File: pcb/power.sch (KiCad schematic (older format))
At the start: 15 parts, among them U6 USBMICROCONN

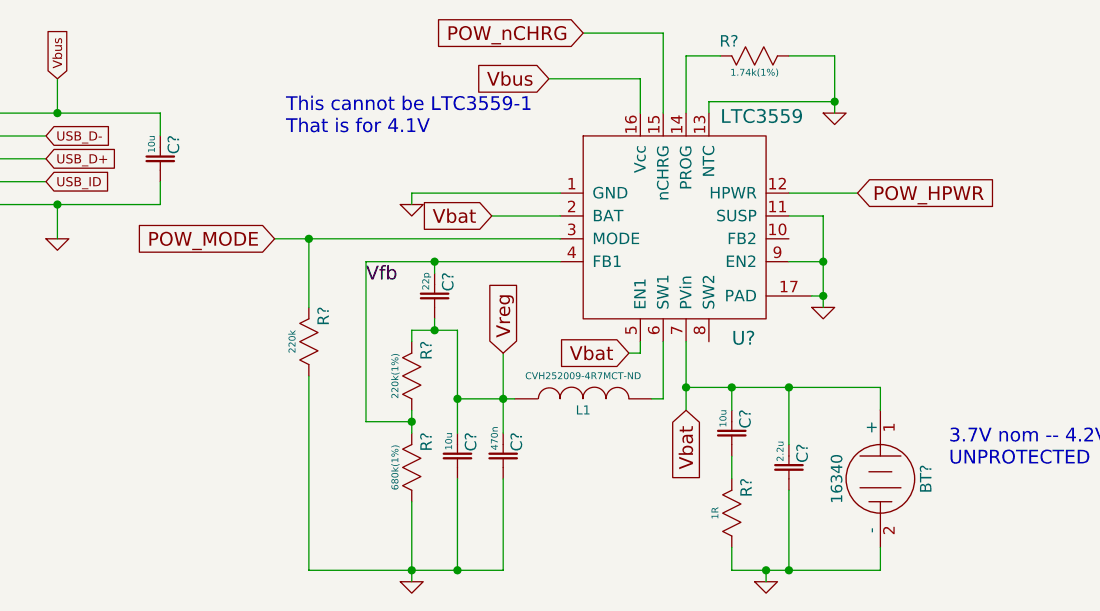
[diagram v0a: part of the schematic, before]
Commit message: Added LCD and started wiring busses
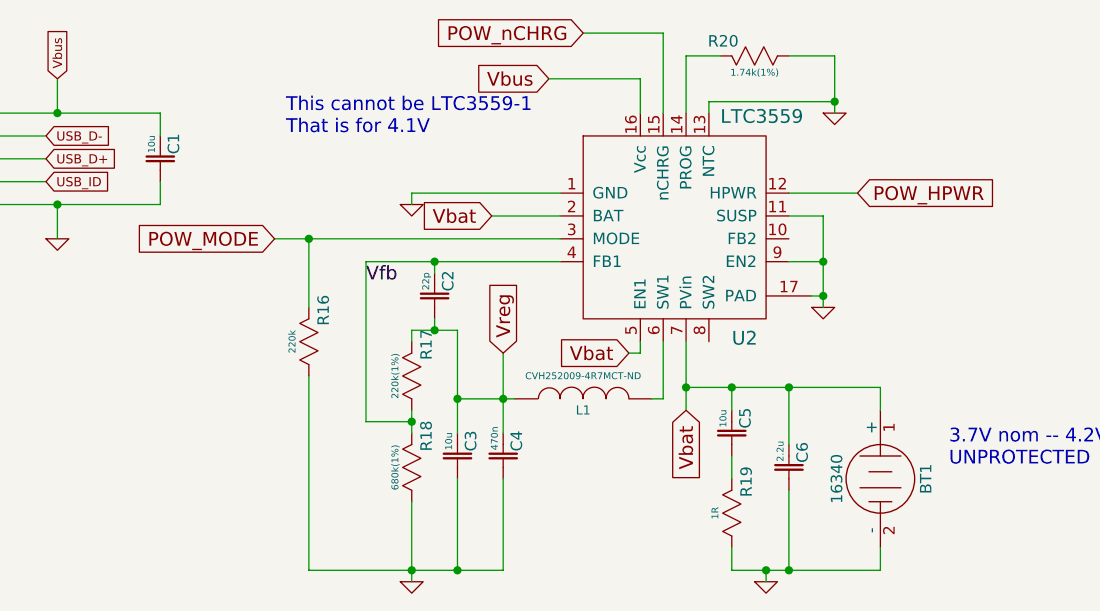
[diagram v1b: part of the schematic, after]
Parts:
- gave numbers to parts that had none: 13
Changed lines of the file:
@@
-EESchema Schematic File Version 2  date Thu 26 Jul 2012 02:08:52 PM EDT
+EESchema Schematic File Version 2  date Thu 26 Jul 2012 11:54:13 PM EDT
 LIBS:power
 LIBS:device
@@
 EELAYER 25  0
 EELAYER END
-$Descr A4 11700 8267
+$Descr A4 11693 8268
 encoding utf-8
 Sheet 4 5
 Title ""
-Date "26 jul 2012"
+Date "27 jul 2012"
 Rev ""
 Comp ""
@@
 Connection ~ 5900 3300
 $Comp
-L BATTERY BT?
+L BATTERY BT1
 U 1 1 501184C6
 P 6300 3700
-F 0 "BT?" H 6300 3900 50  0000 C CNN
+F 0 "BT1" H 6300 3900 50  0000 C CNN
 F 1 "16340" H 6300 3510 50  0000 C CNN
 	1    6300 3700
@@
 $EndComp
 $Comp
-L GND #PWR?
+L GND #PWR21
 U 1 1 50117654
 P 5800 4150
-F 0 "#PWR?" H 5800 4150 30  0001 C CNN
+F 0 "#PWR21" H 5800 4150 30  0001 C CNN
 F 1 "GND" H 5800 4080 30  0001 C CNN
 	1    5800 4150
@@
 $EndComp
 $Comp
-L CAP C?
+L CAP C3
 U 1 1 5011763D
 P 4450 3600
-F 0 "C?" H 4470 3570 50  0000 L TNN
+F 0 "C3" H 4470 3570 50  0000 L TNN
 F 1 "10u" H 4475 3620 30  0000 L BNN
 	1    4450 3600
@@
 $EndComp
 $Comp
-L CAP C?
+L CAP C6
 U 1 1 5011763B
 P 5900 3650
-F 0 "C?" H 5920 3620 50  0000 L TNN
+F 0 "C6" H 5920 3620 50  0000 L TNN
 F 1 "2.2u" H 5925 3670 30  0000 L BNN
 	1    5900 3650
@@
 POW_MODE
 $Comp
-L RES R?
+L RES R16
 U 1 1 501174F2
 P 3800 3100
-F 0 "R?" H 3870 3065 50  0000 L TNN
+F 0 "R16" H 3870 3065 50  0000 L TNN
 F 1 "220k" H 3800 3155 30  0000 C BNN
 	1    3800 3100
@@
 $EndComp
 $Comp
-L RES R?
+L RES R19
 U 1 1 5011722B
 P 5650 3850
-F 0 "R?" H 5720 3815 50  0000 L TNN
+F 0 "R19" H 5720 3815 50  0000 L TNN
 F 1 "1R" H 5650 3905 30  0000 C BNN
 	1    5650 3850
@@
 $EndComp
 $Comp
-L CAP C?
+L CAP C1
 U 1 1 50116F2D
 P 3150 2300
-F 0 "C?" H 3170 2270 50  0000 L TNN
+F 0 "C1" H 3170 2270 50  0000 L TNN
 F 1 "10u" H 3175 2320 30  0000 L BNN
 	1    3150 2300
@@
 Vbat
 $Comp
-L CAP C?
+L CAP C4
 U 1 1 50116EB4
 P 4650 3600
-F 0 "C?" H 4670 3570 50  0000 L TNN
+F 0 "C4" H 4670 3570 50  0000 L TNN
 F 1 "470n" H 4675 3620 30  0000 L BNN
 	1    4650 3600
@@
 $EndComp
 $Comp
-L CAP C?
+L CAP C2
 U 1 1 50116E87
 P 4350 2900
-F 0 "C?" H 4370 2870 50  0000 L TNN
+F 0 "C2" H 4370 2870 50  0000 L TNN
 F 1 "22p" H 4375 2920 30  0000 L BNN
 	1    4350 2900
@@
 Vreg
 $Comp
-L CAP C?
+L CAP C5
 U 1 1 50116E51
 P 5650 3500
-F 0 "C?" H 5670 3470 50  0000 L TNN
+F 0 "C5" H 5670 3470 50  0000 L TNN
 F 1 "10u" H 5675 3520 30  0000 L BNN
 	1    5650 3500
@@
 Vbus
 $Comp
-L GND #PWR?
+L GND #PWR23
 U 1 1 50116DE1
 P 6100 2100
-F 0 "#PWR?" H 6100 2100 30  0001 C CNN
+F 0 "#PWR23" H 6100 2100 30  0001 C CNN
 F 1 "GND" H 6100 2030 30  0001 C CNN
 	1    6100 2100
@@
 $EndComp
 $Comp
-L RES R?
+L RES R20
 U 1 1 50116DC3
 P 5750 1850
-F 0 "R?" H 5820 1815 50  0000 L TNN
+F 0 "R20" H 5820 1815 50  0000 L TNN
 F 1 "1.74k(1%)" H 5750 1905 30  0000 C BNN
 	1    5750 1850
@@
 Vfb
 $Comp
-L GND #PWR?
+L GND #PWR20
 U 1 1 50116D88
 P 4250 4150
-F 0 "#PWR?" H 4250 4150 30  0001 C CNN
+F 0 "#PWR20" H 4250 4150 30  0001 C CNN
 F 1 "GND" H 4250 4080 30  0001 C CNN
 	1    4250 4150
@@
 $EndComp
 $Comp
-L RES R?
+L RES R18
 U 1 1 50116D7E
 P 4250 3650
-F 0 "R?" H 4320 3615 50  0000 L TNN
+F 0 "R18" H 4320 3615 50  0000 L TNN
 F 1 "680k(1%)" H 4250 3705 30  0000 C BNN
 	1    4250 3650
@@
 $EndComp
 $Comp
-L RES R?
+L RES R17
 U 1 1 50116D75
 P 4250 3250
-F 0 "R?" H 4320 3215 50  0000 L TNN
+F 0 "R17" H 4320 3215 50  0000 L TNN
 F 1 "220k(1%)" H 4250 3305 30  0000 C BNN
 	1    4250 3250
@@
 Vbat
 $Comp
-L GND #PWR?
+L GND #PWR22
 U 1 1 50116D38
 P 6050 2950
-F 0 "#PWR?" H 6050 2950 30  0001 C CNN
+F 0 "#PWR22" H 6050 2950 30  0001 C CNN
 F 1 "GND" H 6050 2880 30  0001 C CNN
 	1    6050 2950
@@
 $EndComp
 $Comp
-L GND #PWR?
+L GND #PWR19
 U 1 1 50116D32
 P 4250 2500
-F 0 "#PWR?" H 4250 2500 30  0001 C CNN
+F 0 "#PWR19" H 4250 2500 30  0001 C CNN
 F 1 "GND" H 4250 2430 30  0001 C CNN
 	1    4250 2500
@@
 Vbat
 $Comp
-L LTC3559 U?
+L LTC3559 U2
 U 1 1 50116CFF
 P 5400 2600
-F 0 "U?" H 5650 2150 60  0000 L TNN
+F 0 "U2" H 5650 2150 60  0000 L TNN
 F 1 "LTC3559" H 5600 3050 60  0000 L BNN
 	1    5400 2600

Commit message: Broke up schematic in a more modular fashion -- Added LCD footprint
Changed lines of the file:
@@
-EESchema Schematic File Version 2  date Thu 26 Jul 2012 11:54:13 PM EDT
+EESchema Schematic File Version 2  date Tue 31 Jul 2012 10:29:35 PM EDT
 LIBS:power
 LIBS:device
@@
 EELAYER 25  0
 EELAYER END
-$Descr A4 11693 8268
+$Descr A4 11700 8267
 encoding utf-8
-Sheet 4 5
+Sheet 5 6
 Title ""
-Date "27 jul 2012"
+Date "1 aug 2012"
 Rev ""
 Comp ""
@@
 Comment4 ""
 $EndDescr
+Text HLabel 2650 2400 2    40   Output ~ 0
+USB_ID
+Text HLabel 2650 2300 2    40   Output ~ 0
+USB_D+
+Text HLabel 2650 2200 2    40   Output ~ 0
+USB_D-
+Text HLabel 3650 2650 0    60   Input ~ 0
+POW_MODE
+Text HLabel 5000 1750 0    60   Output ~ 0
+POW_nCHRG
+Text HLabel 6200 2450 2    60   Input ~ 0
+POW_HPWR
 Text Notes 3700 2200 0    60   ~ 0
 This cannot be LTC3559-1\nThat is for 4.1V
@@
 Connection ~ 5900 4100
 Wire Wire Line
-	6300 4100 5900 4100
-Wire Wire Line
-	5900 4100 5800 4100
-Wire Wire Line
-	5800 4100 5650 4100
+	6300 4100 5650 4100
 Wire Wire Line
 	6300 4100 6300 4000
@@
 Connection ~ 3800 2650
 Wire Wire Line
-	4900 2650 3800 2650
-Wire Wire Line
-	3800 2650 3650 2650
+	4900 2650 3650 2650
 Wire Wire Line
 	3800 2650 3800 2950
@@
 	3150 2400 3150 2500
 Wire Wire Line
-	3150 2500 2700 2500
-Wire Wire Line
-	2700 2500 2400 2500
+	3150 2500 2400 2500
 Wire Wire Line
 	3150 2200 3150 2100
@@
 	5900 1850 6100 1850
 Wire Wire Line
-	6100 1850 6100 2050
-Wire Wire Line
-	6100 2050 6100 2100
+	6100 1850 6100 2100
 Wire Wire Line
 	5600 1850 5450 1850
@@
 	5450 1850 5450 2100
 Wire Wire Line
-	4250 3800 4250 4100
-Wire Wire Line
-	4250 4100 4250 4150
+	4250 3800 4250 4150
 Wire Wire Line
 	4250 3100 4250 3050
 Wire Wire Line
-	4250 3050 4350 3050
-Wire Wire Line
-	4350 3050 4450 3050
-Wire Wire Line
-	4700 3350 4650 3350
-Wire Wire Line
-	4650 3350 4450 3350
+	4250 3050 4450 3050
+Wire Wire Line
+	4700 3350 4450 3350
 Wire Wire Line
 	5250 3100 5250 3150
@@
 	5350 3350 5350 3100
 Wire Wire Line
-	4250 3400 4250 3450
-Wire Wire Line
-	4250 3450 4250 3500
+	4250 3400 4250 3500
 Wire Wire Line
 	4250 3450 4050 3450
@@
 	4050 3450 4050 2750
 Wire Wire Line
-	4050 2750 4350 2750
-Wire Wire Line
-	4350 2750 4900 2750
+	4050 2750 4900 2750
 Wire Wire Line
 	5550 2100 5550 2050
@@
 	5250 1950 5250 2100
 Wire Wire Line
-	4450 3050 4450 3350
-Wire Wire Line
-	4450 3350 4450 3500
+	4450 3050 4450 3500
 Connection ~ 4450 3350
 Wire Wire Line
@@
 Connection ~ 4350 2750
 Wire Wire Line
-	4650 3150 4650 3350
-Wire Wire Line
-	4650 3350 4650 3500
-Wire Wire Line
-	5450 3100 5450 3300
-Wire Wire Line
-	5450 3300 5450 3400
+	4650 3150 4650 3500
+Wire Wire Line
+	5450 3100 5450 3400
 Wire Wire Line
 	2700 2650 2700 2500
 Wire Wire Line
-	3150 2100 2700 2100
-Wire Wire Line
-	2700 2100 2400 2100
+	3150 2100 2400 2100
 Wire Wire Line
 	3800 3250 3800 4100
 Wire Wire Line
-	3800 4100 4250 4100
-Wire Wire Line
-	4250 4100 4450 4100
-Wire Wire Line
-	4450 4100 4650 4100
+	3800 4100 4650 4100
 Wire Wire Line
 	5000 1750 5350 1750
@@
 	5900 2550 6050 2550
 Wire Wire Line
-	6050 2550 6050 2750
-Wire Wire Line
-	6050 2750 6050 2900
-Wire Wire Line
-	6050 2900 6050 2950
+	6050 2550 6050 2950
 Connection ~ 6050 2750
 Wire Wire Line
@@
 	6300 3400 6300 3300
 Wire Wire Line
-	6300 3300 5900 3300
-Wire Wire Line
-	5900 3300 5650 3300
-Wire Wire Line
-	5650 3300 5450 3300
+	6300 3300 5450 3300
 Connection ~ 5900 3300
 $Comp
@@
 $EndComp
 $Comp
-L GND #PWR21
+L GND #PWR020
 U 1 1 50117654
 P 5800 4150
-F 0 "#PWR21" H 5800 4150 30  0001 C CNN
+F 0 "#PWR020" H 5800 4150 30  0001 C CNN
 F 1 "GND" H 5800 4080 30  0001 C CNN
 	1    5800 4150
@@
 	0    -1   -1   0
 $EndComp
-Text GLabel 6200 2450 2    60   Input ~ 0
-POW_HPWR
-Text GLabel 5000 1750 0    60   Input ~ 0
-POW_nCHRG
-Text GLabel 3650 2650 0    60   Input ~ 0
-POW_MODE
 $Comp
 L RES R16
@@
 Vbus
 $Comp
-L GND #PWR23
+L GND #PWR021
 U 1 1 50116DE1
 P 6100 2100
-F 0 "#PWR23" H 6100 2100 30  0001 C CNN
+F 0 "#PWR021" H 6100 2100 30  0001 C CNN
 F 1 "GND" H 6100 2030 30  0001 C CNN
 	1    6100 2100
@@
 Vfb
 $Comp
-L GND #PWR20
+L GND #PWR022
 U 1 1 50116D88
 P 4250 4150
-F 0 "#PWR20" H 4250 4150 30  0001 C CNN
+F 0 "#PWR022" H 4250 4150 30  0001 C CNN
 F 1 "GND" H 4250 4080 30  0001 C CNN
 	1    4250 4150
@@
 Vbat
 $Comp
-L GND #PWR22
+L GND #PWR023
 U 1 1 50116D38
 P 6050 2950
-F 0 "#PWR22" H 6050 2950 30  0001 C CNN
+F 0 "#PWR023" H 6050 2950 30  0001 C CNN
 F 1 "GND" H 6050 2880 30  0001 C CNN
 	1    6050 2950
@@
 $EndComp
 $Comp
-L GND #PWR19
+L GND #PWR024
 U 1 1 50116D32
 P 4250 2500
-F 0 "#PWR19" H 4250 2500 30  0001 C CNN
+F 0 "#PWR024" H 4250 2500 30  0001 C CNN
 F 1 "GND" H 4250 2430 30  0001 C CNN
 	1    4250 2500
@@
 	1    0    0    -1
 $EndComp
-Text GLabel 2650 2400 2    40   Input ~ 0
-USB_ID
-Text GLabel 2650 2300 2    40   Input ~ 0
-USB_D+
-Text GLabel 2650 2200 2    40   Input ~ 0
-USB_D-
 Text GLabel 2700 1950 1    40   Input ~ 0
 Vbus
 $Comp
-L GND #PWR18
+L GND #PWR025
 U 1 1 501093EE
 P 2700 2650
-F 0 "#PWR18" H 2700 2650 30  0001 C CNN
+F 0 "#PWR025" H 2700 2650 30  0001 C CNN
 F 1 "GND" H 2700 2580 30  0001 C CNN
 	1    2700 2650

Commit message: Added step-up converter in the schematics files
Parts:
- added C? (x2): 10u, symbol CAP
- added L2: CVH252009-4R7MCT-ND, symbol INDUCTOR
- added R?: 1M, symbol RES
- added R?: 131k, symbol RES
- added U?: TLV61220, symbol TLV61220
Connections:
- net labels added: POW_NXT, Vnxt
- wire segments 60 -> 100
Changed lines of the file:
@@
-EESchema Schematic File Version 2  date Fri 07 Sep 2012 05:49:39 PM EDT
+EESchema Schematic File Version 2  date 9/9/2012 8:55:02 PM
 LIBS:power
 LIBS:device
@@
 Sheet 5 6
 Title ""
-Date "7 sep 2012"
+Date "10 sep 2012"
 Rev ""
 Comp ""
@@
 Comment4 ""
 $EndDescr
+Wire Wire Line
+	8400 2900 8700 2900
+Wire Wire Line
+	8700 2600 7700 2600
+Connection ~ 10100 2600
+Wire Wire Line
+	9900 2900 10100 2900
+Wire Wire Line
+	10000 2300 10000 2100
+Wire Wire Line
+	10000 2300 9900 2300
+Connection ~ 5900 4100
+Wire Wire Line
+	6300 4100 5900 4100
+Wire Wire Line
+	5900 4100 5800 4100
+Wire Wire Line
+	5800 4100 5650 4100
+Wire Wire Line
+	6300 4100 6300 4000
+Connection ~ 5650 3300
+Wire Wire Line
+	5900 3550 5900 3300
+Wire Wire Line
+	5650 3700 5650 3600
+Wire Wire Line
+	5900 4100 5900 3750
+Wire Wire Line
+	5800 4150 5800 4100
+Wire Wire Line
+	6200 2450 5900 2450
+Connection ~ 3800 2650
+Wire Wire Line
+	4900 2650 3800 2650
+Wire Wire Line
+	3800 2650 3650 2650
+Wire Wire Line
+	3800 2650 3800 2950
+Connection ~ 2700 2100
+Wire Wire Line
+	2700 1950 2700 2100
+Connection ~ 2700 2500
+Wire Wire Line
+	3150 2400 3150 2500
+Wire Wire Line
+	3150 2500 2700 2500
+Wire Wire Line
+	2700 2500 2400 2500
+Wire Wire Line
+	3150 2200 3150 2100
+Connection ~ 4450 4100
+Wire Wire Line
+	4650 3700 4650 4100
+Connection ~ 4350 3050
+Wire Wire Line
+	4350 3000 4350 3050
+Connection ~ 4650 3350
+Connection ~ 4250 4100
+Connection ~ 6100 2050
+Wire Wire Line
+	5900 1850 6100 1850
+Wire Wire Line
+	6100 1850 6100 2050
+Wire Wire Line
+	6100 2050 6100 2100
+Wire Wire Line
+	5600 1850 5450 1850
+Wire Wire Line
+	5450 1850 5450 2100
+Wire Wire Line
+	4250 3800 4250 4100
+Wire Wire Line
+	4250 4100 4250 4150
+Wire Wire Line
+	4250 3100 4250 3050
+Wire Wire Line
+	4250 3050 4350 3050
+Wire Wire Line
+	4350 3050 4450 3050
+Wire Wire Line
+	4700 3350 4650 3350
+Wire Wire Line
+	4650 3350 4450 3350
+Wire Wire Line
+	5250 3100 5250 3150
+Wire Wire Line
+	5250 3150 5200 3150
+Wire Wire Line
+	6050 2900 6000 2900
+Wire Wire Line
+	4900 2550 4600 2550
+Wire Wire Line
+	2650 2300 2400 2300
+Wire Wire Line
+	2650 2400 2400 2400
+Wire Wire Line
+	2400 2200 2650 2200
+Wire Wire Line
+	4250 2500 4250 2450
+Wire Wire Line
+	4250 2450 4900 2450
+Wire Wire Line
+	5900 2750 6050 2750
+Connection ~ 6050 2900
+Wire Wire Line
+	5300 3350 5350 3350
+Wire Wire Line
+	5350 3350 5350 3100
+Wire Wire Line
+	4250 3400 4250 3450
+Wire Wire Line
+	4250 3450 4250 3500
+Wire Wire Line
+	4250 3450 4050 3450
+Connection ~ 4250 3450
+Wire Wire Line
+	4050 3450 4050 2750
+Wire Wire Line
+	4050 2750 4350 2750
+Wire Wire Line
+	4350 2750 4900 2750
+Wire Wire Line
+	5550 2100 5550 2050
+Wire Wire Line
+	5550 2050 6100 2050
+Wire Wire Line
+	4850 1950 5250 1950
+Wire Wire Line
+	5250 1950 5250 2100
+Wire Wire Line
+	4450 3050 4450 3350
+Wire Wire Line
+	4450 3350 4450 3500
+Connection ~ 4450 3350
+Wire Wire Line
+	4350 2800 4350 2750
+Connection ~ 4350 2750
+Wire Wire Line
+	4650 3150 4650 3350
+Wire Wire Line
+	4650 3350 4650 3500
+Wire Wire Line
+	5450 3100 5450 3300
+Wire Wire Line
+	5450 3300 5450 3400
+Wire Wire Line
+	2700 2650 2700 2500
+Wire Wire Line
+	3150 2100 2700 2100
+Wire Wire Line
+	2700 2100 2400 2100
+Wire Wire Line
+	3800 3250 3800 4100
+Wire Wire Line
+	3800 4100 4250 4100
+Wire Wire Line
+	4250 4100 4450 4100
+Wire Wire Line
+	4450 4100 4650 4100
+Wire Wire Line
+	5000 1750 5350 1750
+Wire Wire Line
+	5350 1750 5350 2100
+Wire Wire Line
+	5900 2550 6050 2550
+Wire Wire Line
+	6050 2550 6050 2750
+Wire Wire Line
+	6050 2750 6050 2900
+Wire Wire Line
+	6050 2900 6050 2950
+Connection ~ 6050 2750
+Wire Wire Line
+	4450 3700 4450 4100
+Wire Wire Line
+	5650 4100 5650 4000
+Connection ~ 5800 4100
+Wire Wire Line
+	5650 3300 5650 3400
+Connection ~ 5450 3300
+Wire Wire Line
+	6300 3400 6300 3300
+Wire Wire Line
+	6300 3300 5900 3300
+Wire Wire Line
+	5900 3300 5650 3300
+Wire Wire Line
+	5650 3300 5450 3300
+Connection ~ 5900 3300
+Wire Wire Line
+	8700 2300 8400 2300
+Wire Wire Line
+	7800 2300 7700 2300
+Wire Wire Line
+	7700 2300 7600 2300
+Wire Wire Line
+	7600 2300 7600 2100
+Wire Wire Line
+	7700 2300 7700 2400
+Connection ~ 7700 2300
+Connection ~ 7700 2600
+Wire Wire Line
+	10100 2900 10100 3000
+Wire Wire Line
+	10100 3450 10100 3300
+Wire Wire Line
+	10350 2600 10350 2650
+Wire Wire Line
+	10350 3000 10350 2850
+Wire Wire Line
+	10550 2600 10350 2600
+Wire Wire Line
+	10350 2600 10100 2600
+Wire Wire Line
+	10100 2600 9900 2600
+Connection ~ 10350 2600
+Wire Wire Line
+	7700 2600 7700 2800
+Wire Wire Line
+	10000 2100 7600 2100
+Wire Wire Line
+	7600 2100 7500 2100
+Connection ~ 7600 2100
+Text HLabel 8400 2900 0    60   Input ~ 0
+POW_NXT
+Text GLabel 10550 2600 2    60   Output ~ 0
+Vnxt
+Text GLabel 7500 2100 0    60   Input ~ 0
+Vreg
+$Comp
+L GND #PWR?
+U 1 1 504D34F8
+P 10350 3000
+F 0 "#PWR?" H 10350 3000 30  0001 C CNN
+F 1 "GND" H 10350 2930 30  0001 C CNN
+	1    10350 3000
+	1    0    0    -1
+$EndComp
+$Comp
+L CAP C?
+U 1 1 504D34CB
+P 10350 2750
+F 0 "C?" H 10370 2720 50  0000 L TNN
+F 1 "10u" H 10375 2770 30  0000 L BNN
+	1    10350 2750
+	0    -1   -1   0
+$EndComp
+$Comp
+L GND #PWR?
+U 1 1 504D341F
+P 10100 3450
+F 0 "#PWR?" H 10100 3450 30  0001 C CNN
+F 1 "GND" H 10100 3380 30  0001 C CNN
+	1    10100 3450
+	1    0    0    -1
+$EndComp
+$Comp
+L RES R?
+U 1 1 504D340B
+P 10100 3150
+F 0 "R?" H 10170 3115 50  0000 L TNN
+F 1 "131k" H 10100 3205 30  0000 C BNN
+	1    10100 3150
+	0    -1   -1   0
+$EndComp
+$Comp
+L RES R?
+U 1 1 504D33DF
+P 10100 2750
+F 0 "R?" H 10170 2715 50  0000 L TNN
+F 1 "1M" H 10100 2805 30  0000 C BNN
+	1    10100 2750
+	0    -1   -1   0
+$EndComp
+$Comp
+L GND #PWR?
+U 1 1 504D3361
+P 7700 2800
+F 0 "#PWR?" H 7700 2800 30  0001 C CNN
+F 1 "GND" H 7700 2730 30  0001 C CNN
+	1    7700 2800
+	1    0    0    -1
+$EndComp
+$Comp
+L CAP C?
+U 1 1 504D3316
+P 7700 2500
+F 0 "C?" H 7720 2470 50  0000 L TNN
+F 1 "10u" H 7725 2520 30  0000 L BNN
+	1    7700 2500
+	0    1    1    0
+$EndComp
+$Comp
+L INDUCTOR L2
+U 1 1 504D325B
+P 8100 2300
+F 0 "L2" V 8050 2300 40  0000 C CNN
+F 1 "CVH252009-4R7MCT-ND" V 8200 2300 30  0000 C CNN
+	1    8100 2300
+	0    -1   -1   0
+$EndComp
+$Comp
+L TLV61220 U?
+U 1 1 504D3229
+P 9300 2600
+F 0 "U?" H 9250 2200 60  0000 C CNN
+F 1 "TLV61220" H 9300 2450 60  0000 C CNN
+	1    9300 2600
+	1    0    0    -1
+$EndComp
 Text HLabel 2650 2400 2    40   Output ~ 0
 USB_ID
@@
 Text Notes 6600 3650 0    60   ~ 0
 3.7V nom -- 4.2V charge\nUNPROTECTED
-Connection ~ 5900 4100
-Wire Wire Line
-	6300 4100 5650 4100
-Wire Wire Line
-	6300 4100 6300 4000
-Connection ~ 5650 3300
-Wire Wire Line
-	5900 3550 5900 3300
-Wire Wire Line
-	5650 3700 5650 3600
-Wire Wire Line
-	5900 4100 5900 3750
-Wire Wire Line
-	5800 4150 5800 4100
-Wire Wire Line
-	6200 2450 5900 2450
-Connection ~ 3800 2650
-Wire Wire Line
-	4900 2650 3650 2650
-Wire Wire Line
-	3800 2650 3800 2950
-Connection ~ 2700 2100
-Wire Wire Line
-	2700 1950 2700 2100
-Connection ~ 2700 2500
-Wire Wire Line
-	3150 2400 3150 2500
-Wire Wire Line
-	3150 2500 2400 2500
-Wire Wire Line
-	3150 2200 3150 2100
-Connection ~ 4450 4100
-Wire Wire Line
-	4650 3700 4650 4100
-Connection ~ 4350 3050
-Wire Wire Line
-	4350 3000 4350 3050
-Connection ~ 4650 3350
-Connection ~ 4250 4100
-Connection ~ 6100 2050
-Wire Wire Line
-	5900 1850 6100 1850
-Wire Wire Line
-	6100 1850 6100 2100
-Wire Wire Line
-	5600 1850 5450 1850
-Wire Wire Line
-	5450 1850 5450 2100
-Wire Wire Line
-	4250 3800 4250 4150
-Wire Wire Line
-	4250 3100 4250 3050
-Wire Wire Line
-	4250 3050 4450 3050
-Wire Wire Line
-	4700 3350 4450 3350
-Wire Wire Line
-	5250 3100 5250 3150
-Wire Wire Line
-	5250 3150 5200 3150
-Wire Wire Line
-	6050 2900 6000 2900
-Wire Wire Line
-	4900 2550 4600 2550
-Wire Wire Line
-	2650 2300 2400 2300
-Wire Wire Line
-	2650 2400 2400 2400
-Wire Wire Line
-	2400 2200 2650 2200
-Wire Wire Line
-	4250 2500 4250 2450
-Wire Wire Line
-	4250 2450 4900 2450
-Wire Wire Line
-	5900 2750 6050 2750
-Connection ~ 6050 2900
-Wire Wire Line
-	5300 3350 5350 3350
-Wire Wire Line
-	5350 3350 5350 3100
-Wire Wire Line
-	4250 3400 4250 3500
-Wire Wire Line
-	4250 3450 4050 3450
-Connection ~ 4250 3450
-Wire Wire Line
-	4050 3450 4050 2750
-Wire Wire Line
-	4050 2750 4900 2750
-Wire Wire Line
-	5550 2100 5550 2050
-Wire Wire Line
-	5550 2050 6100 2050
-Wire Wire Line
-	4850 1950 5250 1950
-Wire Wire Line
-	5250 1950 5250 2100
-Wire Wire Line
-	4450 3050 4450 3500
-Connection ~ 4450 3350
-Wire Wire Line
-	4350 2800 4350 2750
-Connection ~ 4350 2750
-Wire Wire Line
-	4650 3150 4650 3500
-Wire Wire Line
-	5450 3100 5450 3400
-Wire Wire Line
-	2700 2650 2700 2500
-Wire Wire Line
-	3150 2100 2400 2100
-Wire Wire Line
-	3800 3250 3800 4100
-Wire Wire Line
-	3800 4100 4650 4100
-Wire Wire Line
-	5000 1750 5350 1750
-Wire Wire Line
-	5350 1750 5350 2100
-Wire Wire Line
-	5900 2550 6050 2550
-Wire Wire Line
-	6050 2550 6050 2950
-Connection ~ 6050 2750
-Wire Wire Line
-	4450 3700 4450 4100
-Wire Wire Line
-	5650 4100 5650 4000
-Connection ~ 5800 4100
-Wire Wire Line
-	5650 3300 5650 3400
-Connection ~ 5450 3300
-Wire Wire Line
-	6300 3400 6300 3300
-Wire Wire Line
-	6300 3300 5450 3300
-Connection ~ 5900 3300
 $Comp
 L BATTERY BT1
